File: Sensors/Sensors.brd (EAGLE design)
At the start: 101.6 x 53.3 mm, 34 parts, among them J2 JST_CONNECTOR, J6 JST_CONNECTOR, J7 JST_CONNECTOR, J8 JST_CONNECTOR, J9 JST_CONNECTOR

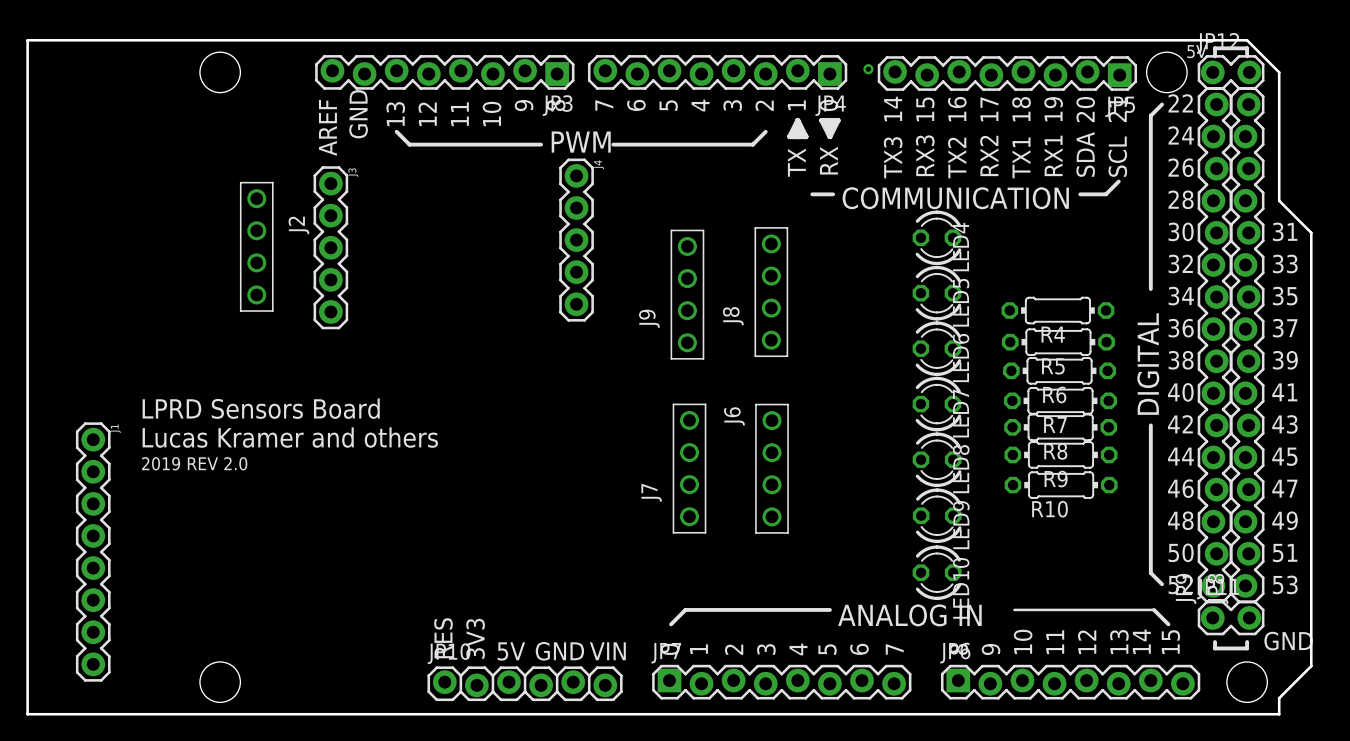
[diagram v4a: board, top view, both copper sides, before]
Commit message: Finished routing, added accelerometer LED
UMN Logo is on wrong side, but such is life.
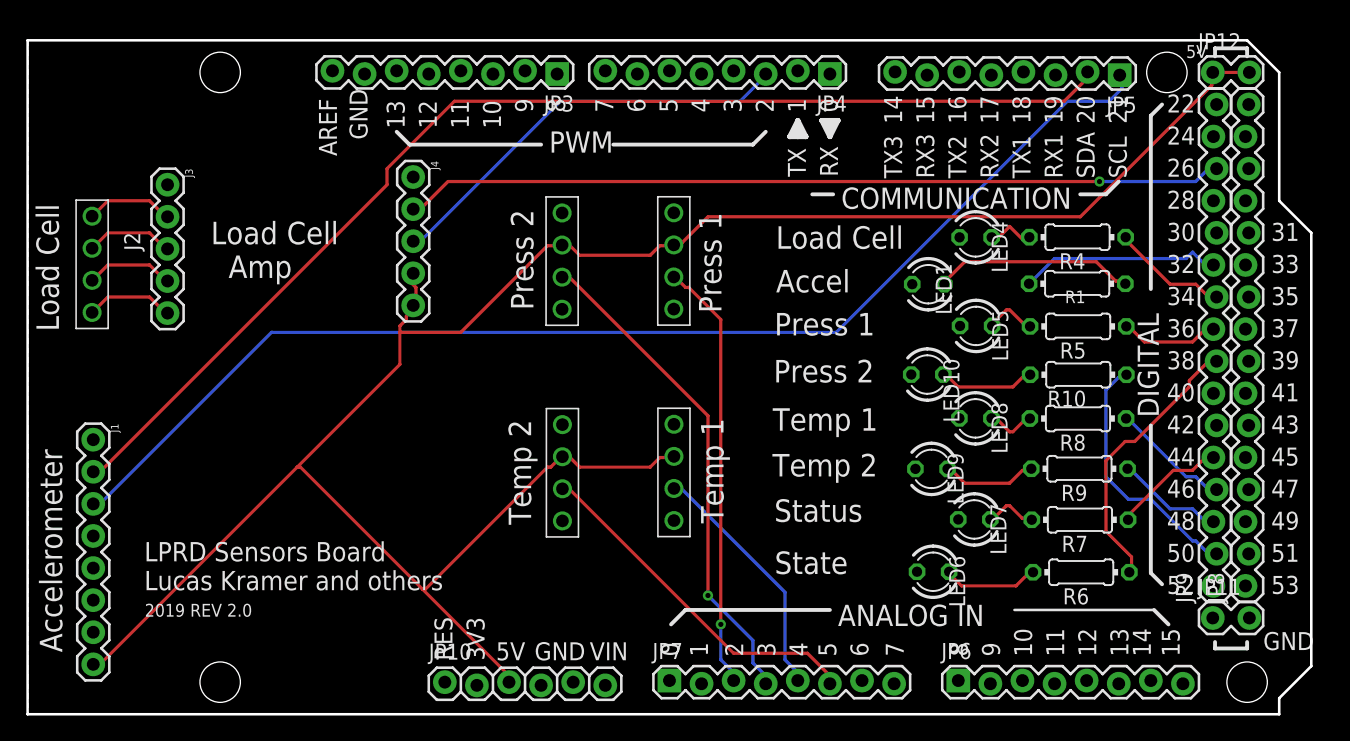
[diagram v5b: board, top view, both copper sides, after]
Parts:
- removed U$1: (no value), UMNLogo:UMNLOGO
- added LED1: (no value), led:LED3MM
- added R1: 1000, rcl:0204/7
- added T$1: (no value), UMNLogo:UMNLOGO
- moved LED6 17.7 mm to (71.7, 11.3)
- moved R6 16.0 mm to (83.4, 11.2)
- moved LED10 15.7 mm to (71.2, 26.9)
- moved U$2 13.4 mm to (40.7, 16.7)
- moved J2 13.1 mm to (5.11, 34.3)
- moved J3 12.9 mm to (11.1, 41.9)
- moved J4 12.9 mm to (30.5, 42.5)
- moved J9 10.3 mm to (42.3, 37.1)
- moved J7 10.1 mm to (42.3, 20.4)
- moved LED7 9.60 mm to (74.9, 15.4)
- moved R7 9.54 mm to (83.3, 15.4)
- moved R10 8.84 mm to (83.2, 26.9)
- moved J8 8.11 mm to (51.1, 37.1)
- moved J6 7.77 mm to (51.2, 20.4)
- moved R4 6.01 mm to (83.1, 37.8)
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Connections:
- net D40 renamed D34
- removed net D38: JP9.8
- removed net D42: JP9.11
- new net ACCEL_LED: JP9.11, R1.1
- new net D32: JP9.6
- new net N$1: LED1.A, R1.2
- net GND: now also LED1.K
- net STATE_LED: now also JP9.8; no longer JP9.6
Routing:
- net 5V: track 0.00 -> 168.2 mm
- net SCL: track 0.00 -> 96.2 mm
- net SDA: track 0.00 -> 92.8 mm, vias 1 -> 0
- net FORCE_CLK: track 0.00 -> 64.9 mm, vias 0 -> 1
- net VOUT_PRESSURE_2: track 0.00 -> 39.2 mm, vias 0 -> 1
- net VOUT_PRESSURE_1: track 0.00 -> 34.1 mm, vias 0 -> 1
- net FORCE_DAT: track 0.00 -> 33.4 mm
- net VOUT_TEMPERATURE_2: track 0.00 -> 27.9 mm
- net STATE_LED: track 0.00 -> 22.1 mm
- net PRESSURE2_LED: track 0.00 -> 20.3 mm
- net VOUT_TEMPERATURE_1: track 0.00 -> 19.6 mm
- net N$1: track 0.00 -> 16.0 mm
- net ACCEL_LED: track 0.00 -> 16.0 mm
- net TEMP1_LED: track 0.00 -> 9.48 mm
- net FORCE_LED: track 0.00 -> 9.30 mm
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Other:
- board text added: "Accel"
- board text added: "Accelerometer"
- board text added: "Load Cell"
- board text added: "Load Cell Amp"
- board text added: "Press 1"
- board text added: "Press 2"
- board text added: "State"
- board text added: "Status"
- board text added: "Temp 1"
- board text added: "Temp 2"

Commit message: Rearranged load cell seat, adressed errors
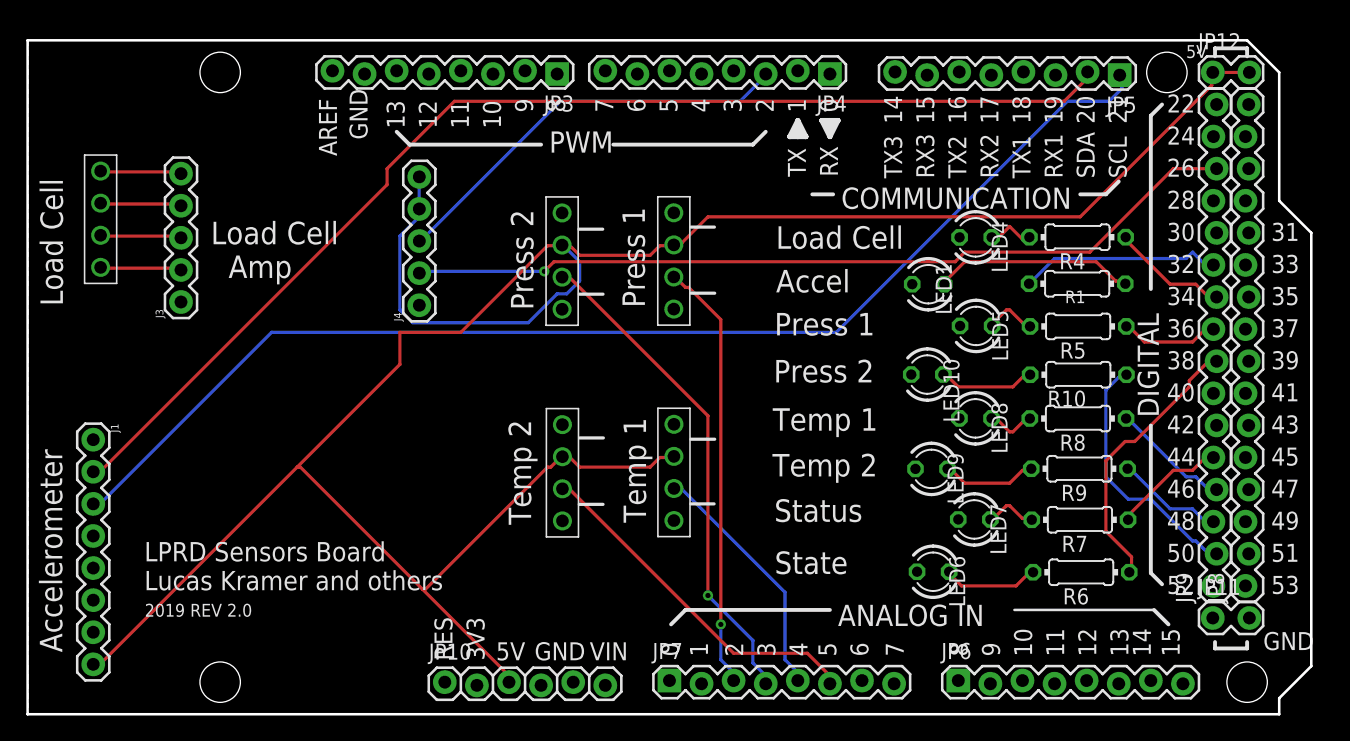
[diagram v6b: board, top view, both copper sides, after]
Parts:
- moved J4 10.2 mm to (31.0, 32.4), turned to 90 degrees
- moved J3 9.34 mm to (12.1, 32.6), turned to 90 degrees
- moved J2 6.15 mm to (5.78, 40.4), turned to 90 degrees
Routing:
- net 5V: track 168.2 -> 193.3 mm
- net FORCE_CLK: track 64.9 -> 66.5 mm
- net E+/RED: track 6.99 -> 6.43 mm
- net E-/BLACK: track 6.99 -> 6.43 mm
- net A-/WHITE: track 6.99 -> 6.43 mm
- net A+/GREEN: track 6.99 -> 6.43 mm

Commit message: Misc. minor tweaks to routing, layout and labels
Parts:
- moved U$2 37.2 mm to (6.13, 2.90)
- moved T$1 2.02 mm to (9.51, 16.0)
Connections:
- net MAXCLK renamed D22
- net MAXCS1 renamed D52
- net MAXDO renamed D50
- net PRESSURE1_LED renamed PRESSURE_FUEL_LED
- net PRESSURE2_LED renamed PRESSURE_OX_LED
- net TEMP1_LED renamed TEMP_OUT_LED
- net TEMP2_LED renamed TEMP_IN_LED
- net VOUT_PRESSURE_1 renamed VOUT_PRESSURE_FUEL
- net VOUT_PRESSURE_2 renamed VOUT_PRESSURE_OX
- net VOUT_TEMPERATURE_1 renamed VOUT_TEMPERATURE_OUT
- net VOUT_TEMPERATURE_2 renamed VOUT_TEMPERATURE_IN
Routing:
- net 5V: track 193.3 -> 171.3 mm
- net N$5: track 4.45 -> 3.25 mm
- net N$6: track 7.89 -> 6.83 mm
- net N$4: track 3.88 -> 3.04 mm
- net N$7: track 4.22 -> 3.37 mm
- net PRESSURE_FUEL_LED: track 7.84 -> 7.00 mm
- net N$15: track 4.14 -> 3.30 mm
- net N$16: track 7.57 -> 6.74 mm
- net N$23: track 7.73 -> 7.10 mm
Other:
- board text added: "Press Fuel"
- board text added: "Press Ox"
- board text added: "Temp In"
- board text added: "Temp Out"
- board text removed: "Press 1"
- board text removed: "Press 2"
- board text removed: "Temp 1"
- board text removed: "Temp 2"

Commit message: Some changes that I forgot to push yesterday
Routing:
- net 5V: track 171.3 -> 146.1 mm
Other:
- board text added: "Press 1"
- board text added: "Press 2"
- board text added: "Temp 1"
- board text added: "Temp 2"
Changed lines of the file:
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@@
 <text x="59.2201" y="36.8427" size="1.778" layer="21">Load Cell</text>
 <text x="59.1058" y="29.9847" size="1.778" layer="21">Press Fuel</text>
-<text x="48.7045" y="30.6197" size="1.778" layer="21" rot="R90">Press Fuel</text>
+<text x="48.8569" y="32.1818" size="1.778" layer="21" rot="R90">Press 1</text>
 <text x="59.0423" y="26.2636" size="1.778" layer="21">Press Ox</text>
-<text x="39.6621" y="30.7467" size="1.778" layer="21" rot="R90">Press Ox</text>
+<text x="40.0304" y="31.9913" size="1.778" layer="21" rot="R90">Press 2</text>
 <text x="58.9788" y="22.4409" size="1.778" layer="21">Temp Out</text>
-<text x="49.0601" y="14.6558" size="1.778" layer="21" rot="R90">Temp Out</text>
+<text x="48.9458" y="15.1638" size="1.778" layer="21" rot="R90">Temp 1</text>
 <text x="58.9534" y="18.8214" size="1.778" layer="21">Temp In</text>
-<text x="39.7637" y="14.859" size="1.778" layer="21" rot="R90">Temp In</text>
+<text x="39.8526" y="14.9987" size="1.778" layer="21" rot="R90">Temp 2</text>
 <text x="59.0931" y="15.2273" size="1.778" layer="21">Status</text>
 <text x="59.1185" y="11.0998" size="1.778" layer="21">State</text>
@@
 <wire x1="42.418" y1="20.32" x2="42.3291" y2="20.3835" width="0.254" layer="1"/>
 <wire x1="51.054" y1="20.32" x2="51.1556" y2="20.4089" width="0.254" layer="1"/>
-<wire x1="21.22805" y1="19.97075" x2="5.26415" y2="4.00685" width="0.254" layer="1"/>
+<wire x1="20.5232" y1="19.2659" x2="20.4089" y2="19.1516" width="0.254" layer="1"/>
+<wire x1="20.4089" y1="19.1516" x2="5.26415" y2="4.00685" width="0.254" layer="1"/>
 <wire x1="5.26415" y1="4.00685" x2="5.1943" y2="3.9497" width="0.254" layer="1"/>
 <wire x1="38.1" y1="3.048" x2="38.1" y2="2.54" width="0.254" layer="1"/>
+<wire x1="31.2928" y1="9.906" x2="21.3233" y2="19.8755" width="0.254" layer="1"/>
 <wire x1="31.242" y1="9.906" x2="38.1" y2="3.048" width="0.254" layer="1"/>
 <wire x1="31.75" y1="9.906" x2="42.164" y2="20.32" width="0.254" layer="1"/>
@@
 <wire x1="42.164" y1="20.32" x2="42.3291" y2="20.3835" width="0.254" layer="1"/>
 <wire x1="42.164" y1="37.084" x2="42.3037" y2="37.1348" width="0.254" layer="1"/>
-<wire x1="42.164" y1="37.084" x2="38.3413" y2="37.084" width="0.254" layer="1"/>
-<wire x1="38.3413" y1="37.084" x2="33.909" y2="37.084" width="0.254" layer="1"/>
+<wire x1="30.988" y1="42.418" x2="31.0007" y2="42.5323" width="0.254" layer="16"/>
+<wire x1="42.164" y1="37.084" x2="38.5318" y2="37.084" width="0.254" layer="1"/>
+<wire x1="38.5318" y1="37.084" x2="33.909" y2="37.084" width="0.254" layer="1"/>
 <wire x1="33.909" y1="37.084" x2="31.0007" y2="39.9923" width="0.254" layer="1"/>
 <wire x1="31.0007" y1="39.9923" x2="31.0007" y2="42.5323" width="0.254" layer="1"/>
-<wire x1="21.22805" y1="19.97075" x2="38.3413" y2="37.084" width="0.254" layer="1"/>
-<wire x1="31.2928" y1="9.906" x2="21.22805" y2="19.97075" width="0.254" layer="1"/>
+<wire x1="51.1556" y1="20.4089" x2="51.054" y2="37.084" width="0" layer="19" extent="1-1"/>
+<wire x1="20.4089" y1="19.1516" x2="21.3233" y2="19.8755" width="0" layer="19" extent="1-1"/>
+<wire x1="20.4089" y1="19.1516" x2="20.4089" y2="19.1516" width="0.254" layer="1"/>
 </signal>
 <signal name="GND">
